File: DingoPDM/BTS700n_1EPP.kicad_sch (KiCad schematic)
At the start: 13 parts, among them U5 BTS700n-1EPP

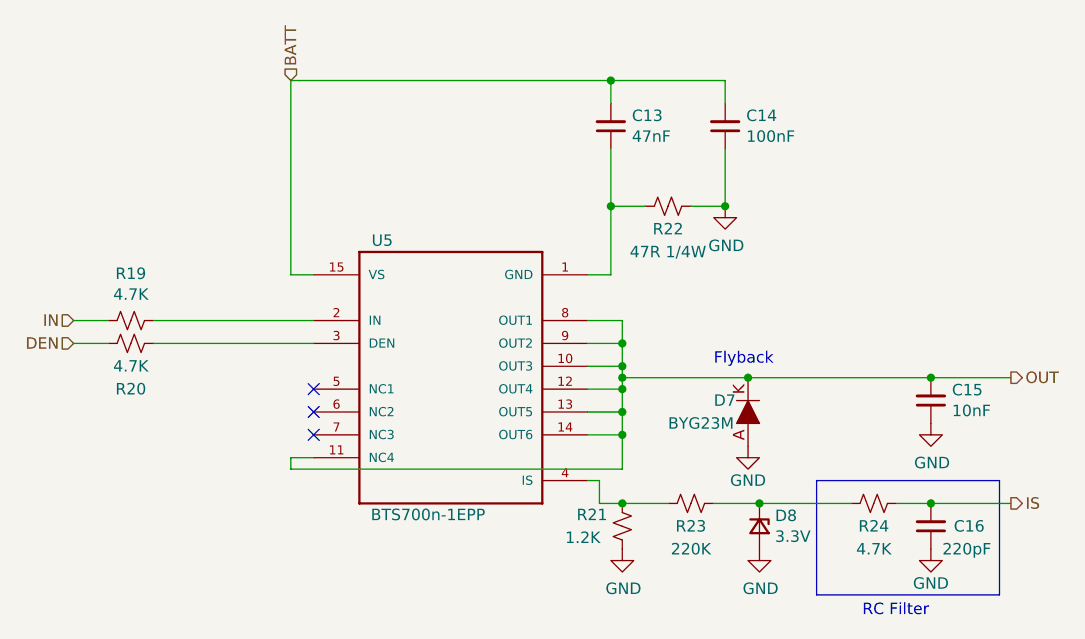
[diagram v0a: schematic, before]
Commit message: Swapped to AMPSEAL 14 pins
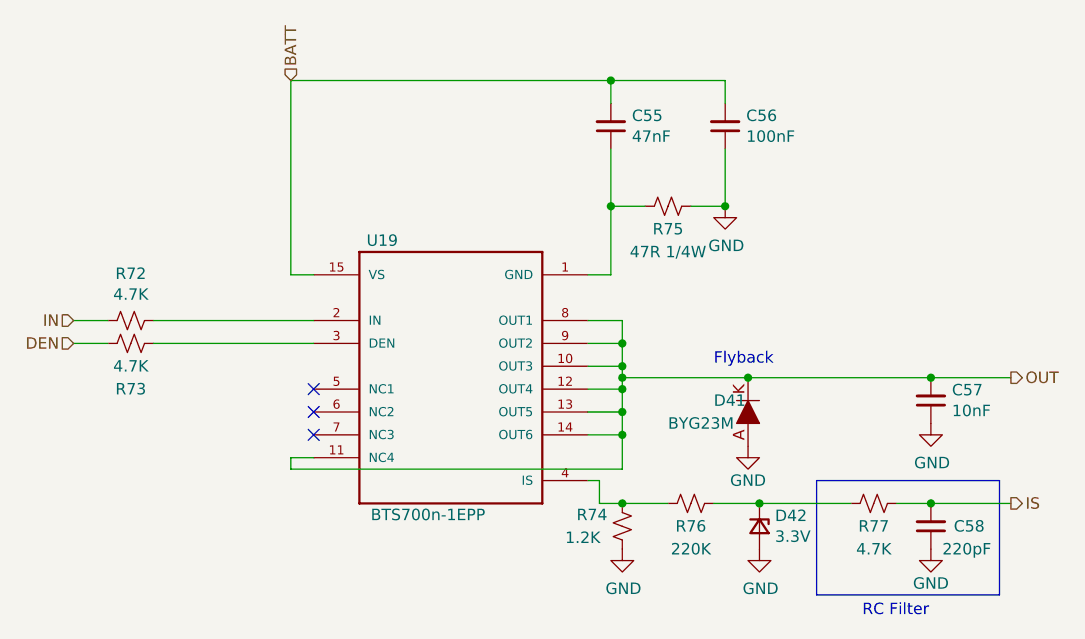
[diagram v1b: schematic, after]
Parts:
- renumbered C13 to C55, C14 to C56, C15 to C57, C16 to C58, D7 to D41, D8 to D42, R19 to R72, R20 to R73, R21 to R74, R22 to R75, R23 to R76, R24 to R77, U5 to U19
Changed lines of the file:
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@@
     (effects (font (size 1.27 1.27)) (justify right))
   )
-  (symbol (lib_id "Device:R_Small_US") (at 96.52 90.17 270)
-    (in_bom yes) (on_board yes)
-    (property "Reference" "R19" (id 0) (at 96.52 84.963 90))
+  (symbol (lib_id "Device:R_Small_US") (at 96.52 90.17 270) (unit 1)
+    (in_bom yes) (on_board yes)
+    (property "Reference" "R72" (id 0) (at 96.52 84.963 90))
     (property "Value" "4.7K" (id 1) (at 96.52 87.2744 90))
     (property "Footprint" "Resistor_SMD:R_0805_2012Metric" (id 2) (at 96.52 90.17 0)
@@
     (pin "2")
   )
-  (symbol (lib_id "Device:R_Small_US") (at 96.52 92.71 270)
-    (in_bom yes) (on_board yes)
-    (property "Reference" "R20" (id 0) (at 96.52 97.79 90))
+  (symbol (lib_id "Device:R_Small_US") (at 96.52 92.71 270) (unit 1)
+    (in_bom yes) (on_board yes)
+    (property "Reference" "R73" (id 0) (at 96.52 97.79 90))
     (property "Value" "4.7K" (id 1) (at 96.52 95.25 90))
     (property "Footprint" "Resistor_SMD:R_0805_2012Metric" (id 2) (at 96.52 92.71 0)
@@
     (pin "2")
   )
-  (symbol (lib_id "Device:C_Small") (at 162.56 68.58 180)
-    (in_bom yes) (on_board yes)
-    (property "Reference" "C14" (id 0) (at 164.8968 67.4116 0)
+  (symbol (lib_id "Device:C_Small") (at 162.56 68.58 180) (unit 1)
+    (in_bom yes) (on_board yes)
+    (property "Reference" "C56" (id 0) (at 164.8968 67.4116 0)
       (effects (font (size 1.27 1.27)) (justify right))
     )
@@
     (pin "2")
   )
-  (symbol (lib_id "Device:C_Small") (at 149.86 68.58 180)
-    (in_bom yes) (on_board yes)
-    (property "Reference" "C13" (id 0) (at 152.1968 67.4116 0)
+  (symbol (lib_id "Device:C_Small") (at 149.86 68.58 180) (unit 1)
+    (in_bom yes) (on_board yes)
+    (property "Reference" "C55" (id 0) (at 152.1968 67.4116 0)
       (effects (font (size 1.27 1.27)) (justify right))
     )
@@
     (pin "2")
   )
-  (symbol (lib_id "Device:R_Small_US") (at 156.21 77.47 270)
-    (in_bom yes) (on_board yes)
-    (property "Reference" "R22" (id 0) (at 156.21 80.01 90))
+  (symbol (lib_id "Device:R_Small_US") (at 156.21 77.47 270) (unit 1)
+    (in_bom yes) (on_board yes)
+    (property "Reference" "R75" (id 0) (at 156.21 80.01 90))
     (property "Value" "47R 1/4W" (id 1) (at 156.21 82.55 90))
     (property "Footprint" "Resistor_SMD:R_1206_3216Metric" (id 2) (at 156.21 77.47 0)
@@
     (pin "2")
   )
-  (symbol (lib_id "power:GND") (at 162.56 77.47 0)
-    (in_bom yes) (on_board yes)
-    (property "Reference" "#PWR026" (id 0) (at 162.56 83.82 0)
+  (symbol (lib_id "power:GND") (at 162.56 77.47 0) (unit 1)
+    (in_bom yes) (on_board yes)
+    (property "Reference" "#PWR0156" (id 0) (at 162.56 83.82 0)
       (effects (font (size 1.27 1.27)) hide)
     )
@@
     (pin "1")
   )
-  (symbol (lib_id "Device:C_Small") (at 185.42 99.06 180)
-    (in_bom yes) (on_board yes)
-    (property "Reference" "C15" (id 0) (at 187.7568 97.8916 0)
+  (symbol (lib_id "Device:C_Small") (at 185.42 99.06 180) (unit 1)
+    (in_bom yes) (on_board yes)
+    (property "Reference" "C57" (id 0) (at 187.7568 97.8916 0)
       (effects (font (size 1.27 1.27)) (justify right))
     )
@@
     (pin "2")
   )
-  (symbol (lib_id "power:GND") (at 185.42 101.6 0)
-    (in_bom yes) (on_board yes)
-    (property "Reference" "#PWR029" (id 0) (at 185.42 107.95 0)
+  (symbol (lib_id "power:GND") (at 185.42 101.6 0) (unit 1)
+    (in_bom yes) (on_board yes)
+    (property "Reference" "#PWR0159" (id 0) (at 185.42 107.95 0)
       (effects (font (size 1.27 1.27)) hide)
     )
@@
     (pin "1")
   )
-  (symbol (lib_id "Device:R_Small_US") (at 179.07 110.49 270)
-    (in_bom yes) (on_board yes)
-    (property "Reference" "R24" (id 0) (at 179.07 113.03 90))
+  (symbol (lib_id "Device:R_Small_US") (at 179.07 110.49 270) (unit 1)
+    (in_bom yes) (on_board yes)
+    (property "Reference" "R77" (id 0) (at 179.07 113.03 90))
     (property "Value" "4.7K" (id 1) (at 179.07 115.57 90))
     (property "Footprint" "Resistor_SMD:R_0805_2012Metric" (id 2) (at 179.07 110.49 0)
@@
     (pin "2")
   )
-  (symbol (lib_id "Device:C_Small") (at 185.42 113.03 180)
-    (in_bom yes) (on_board yes)
-    (property "Reference" "C16" (id 0) (at 187.96 113.03 0)
+  (symbol (lib_id "Device:C_Small") (at 185.42 113.03 180) (unit 1)
+    (in_bom yes) (on_board yes)
+    (property "Reference" "C58" (id 0) (at 187.96 113.03 0)
       (effects (font (size 1.27 1.27)) (justify right))
     )
@@
     (pin "2")
   )
-  (symbol (lib_id "Device:R_Small_US") (at 151.13 113.03 0)
-    (in_bom yes) (on_board yes)
-    (property "Reference" "R21" (id 0) (at 146.05 111.76 0)
+  (symbol (lib_id "Device:R_Small_US") (at 151.13 113.03 0) (unit 1)
+    (in_bom yes) (on_board yes)
+    (property "Reference" "R74" (id 0) (at 146.05 111.76 0)
       (effects (font (size 1.27 1.27)) (justify left))
     )
@@
     (pin "2")
   )
-  (symbol (lib_id "Device:R_Small_US") (at 158.75 110.49 270)
-    (in_bom yes) (on_board yes)
-    (property "Reference" "R23" (id 0) (at 158.75 113.03 90))
+  (symbol (lib_id "Device:R_Small_US") (at 158.75 110.49 270) (unit 1)
+    (in_bom yes) (on_board yes)
+    (property "Reference" "R76" (id 0) (at 158.75 113.03 90))
     (property "Value" "220K" (id 1) (at 158.75 115.57 90))
     (property "Footprint" "Resistor_SMD:R_0805_2012Metric" (id 2) (at 158.75 110.49 0)
@@
     (pin "2")
   )
-  (symbol (lib_id "Device:D_Zener_Small") (at 166.37 113.03 270)
-    (in_bom yes) (on_board yes)
-    (property "Reference" "D8" (id 0) (at 168.0972 111.8616 90)
+  (symbol (lib_id "Device:D_Zener_Small") (at 166.37 113.03 270) (unit 1)
+    (in_bom yes) (on_board yes)
+    (property "Reference" "D42" (id 0) (at 168.0972 111.8616 90)
       (effects (font (size 1.27 1.27)) (justify left))
     )
@@
     (pin "2")
   )
-  (symbol (lib_id "power:GND") (at 151.13 115.57 0)
-    (in_bom yes) (on_board yes)
-    (property "Reference" "#PWR025" (id 0) (at 151.13 121.92 0)
+  (symbol (lib_id "power:GND") (at 151.13 115.57 0) (unit 1)
+    (in_bom yes) (on_board yes)
+    (property "Reference" "#PWR0155" (id 0) (at 151.13 121.92 0)
       (effects (font (size 1.27 1.27)) hide)
     )
@@
     (pin "1")
   )
-  (symbol (lib_id "power:GND") (at 166.37 115.57 0)
-    (in_bom yes) (on_board yes)
-    (property "Reference" "#PWR028" (id 0) (at 166.37 121.92 0)
+  (symbol (lib_id "power:GND") (at 166.37 115.57 0) (unit 1)
+    (in_bom yes) (on_board yes)
+    (property "Reference" "#PWR0158" (id 0) (at 166.37 121.92 0)
       (effects (font (size 1.27 1.27)) hide)
     )
@@
     (pin "1")
   )
-  (symbol (lib_id "power:GND") (at 185.42 115.57 0)
-    (in_bom yes) (on_board yes)
-    (property "Reference" "#PWR030" (id 0) (at 185.42 121.92 0)
+  (symbol (lib_id "power:GND") (at 185.42 115.57 0) (unit 1)
+    (in_bom yes) (on_board yes)
+    (property "Reference" "#PWR0160" (id 0) (at 185.42 121.92 0)
       (effects (font (size 1.27 1.27)) hide)
     )
@@
     (pin "1")
   )
-  (symbol (lib_id "power:GND") (at 165.1 104.14 0)
-    (in_bom yes) (on_board yes)
-    (property "Reference" "#PWR027" (id 0) (at 165.1 110.49 0)
+  (symbol (lib_id "power:GND") (at 165.1 104.14 0) (unit 1)
+    (in_bom yes) (on_board yes)
+    (property "Reference" "#PWR0157" (id 0) (at 165.1 110.49 0)
       (effects (font (size 1.27 1.27)) hide)
     )
@@
     (pin "1")
   )
-  (symbol (lib_id "Profet:BTS700n-1EPP") (at 121.92 82.55 0)
-    (in_bom yes) (on_board yes)
-    (property "Reference" "U5" (id 0) (at 124.46 81.28 0))
+  (symbol (lib_id "Profet:BTS700n-1EPP") (at 121.92 82.55 0) (unit 1)
+    (in_bom yes) (on_board yes)
+    (property "Reference" "U19" (id 0) (at 124.46 81.28 0))
     (property "Value" "BTS700n-1EPP" (id 1) (at 129.54 111.76 0))
     (property "Footprint" "Profet:TDSO-14" (id 2) (at 121.92 82.55 0)
@@
     (pin "9")
   )
-  (symbol (lib_id "dk_Diodes-Rectifiers-Single:SS14") (at 165.1 99.06 270)
-    (in_bom yes) (on_board yes)
-    (property "Reference" "D7" (id 0) (at 161.29 99.06 90)
-      (effects (font (size 1.27 1.27)) (justify left))
-    )
+  (symbol (lib_id "dk_Diodes-Rectifiers-Single:SS14") (at 165.1 99.06 270) (unit 1)
+    (in_bom yes) (on_board yes)
+    (property "Reference" "D41" (id 0) (at 161.29 99.06 90)
+      (effects (font (size 1.27 1.27)) (justify left))
+    )

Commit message: Removed unused IRQs, added pd res on PF GPIO reset
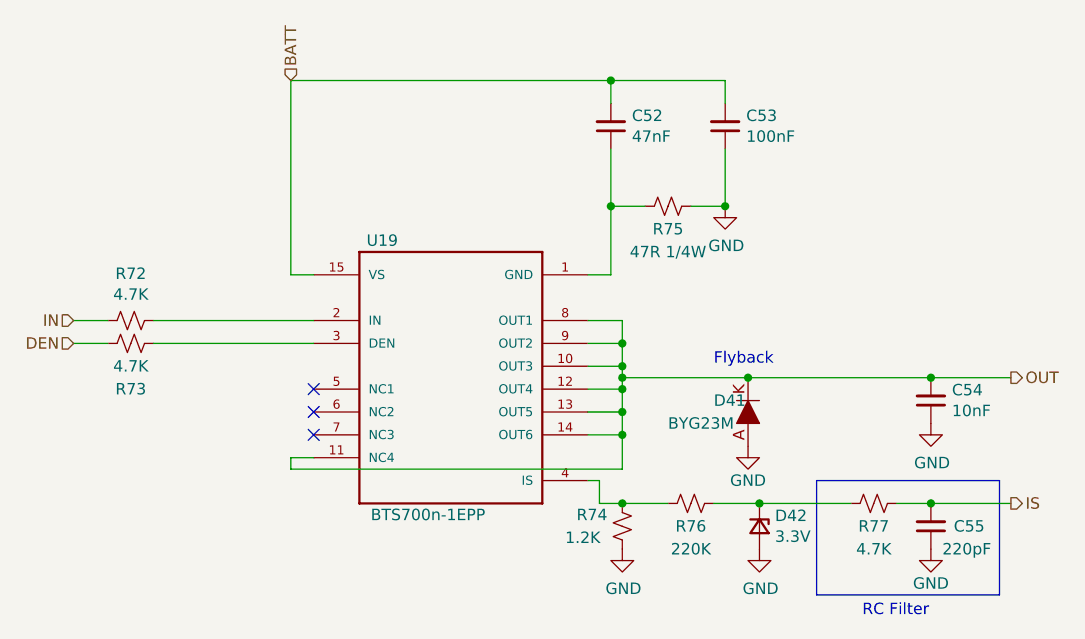
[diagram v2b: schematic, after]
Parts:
- renumbered C55 to C52, C56 to C53, C57 to C54, C58 to C55
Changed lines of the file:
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@@
   (symbol (lib_id "Device:C_Small") (at 162.56 68.58 180) (unit 1)
     (in_bom yes) (on_board yes)
-    (property "Reference" "C56" (id 0) (at 164.8968 67.4116 0)
+    (property "Reference" "C53" (id 0) (at 164.8968 67.4116 0)
       (effects (font (size 1.27 1.27)) (justify right))
     )
@@
   (symbol (lib_id "Device:C_Small") (at 149.86 68.58 180) (unit 1)
     (in_bom yes) (on_board yes)
-    (property "Reference" "C55" (id 0) (at 152.1968 67.4116 0)
+    (property "Reference" "C52" (id 0) (at 152.1968 67.4116 0)
       (effects (font (size 1.27 1.27)) (justify right))
     )
@@
   (symbol (lib_id "power:GND") (at 162.56 77.47 0) (unit 1)
     (in_bom yes) (on_board yes)
-    (property "Reference" "#PWR0156" (id 0) (at 162.56 83.82 0)
+    (property "Reference" "#PWR0153" (id 0) (at 162.56 83.82 0)
       (effects (font (size 1.27 1.27)) hide)
     )
@@
   (symbol (lib_id "Device:C_Small") (at 185.42 99.06 180) (unit 1)
     (in_bom yes) (on_board yes)
-    (property "Reference" "C57" (id 0) (at 187.7568 97.8916 0)
+    (property "Reference" "C54" (id 0) (at 187.7568 97.8916 0)
       (effects (font (size 1.27 1.27)) (justify right))
     )
@@
   (symbol (lib_id "power:GND") (at 185.42 101.6 0) (unit 1)
     (in_bom yes) (on_board yes)
-    (property "Reference" "#PWR0159" (id 0) (at 185.42 107.95 0)
+    (property "Reference" "#PWR0156" (id 0) (at 185.42 107.95 0)
       (effects (font (size 1.27 1.27)) hide)
     )
@@
   (symbol (lib_id "Device:C_Small") (at 185.42 113.03 180) (unit 1)
     (in_bom yes) (on_board yes)
-    (property "Reference" "C58" (id 0) (at 187.96 113.03 0)
+    (property "Reference" "C55" (id 0) (at 187.96 113.03 0)
       (effects (font (size 1.27 1.27)) (justify right))
     )
@@
   (symbol (lib_id "power:GND") (at 151.13 115.57 0) (unit 1)
     (in_bom yes) (on_board yes)
-    (property "Reference" "#PWR0155" (id 0) (at 151.13 121.92 0)
+    (property "Reference" "#PWR0152" (id 0) (at 151.13 121.92 0)
       (effects (font (size 1.27 1.27)) hide)
     )
@@
   (symbol (lib_id "power:GND") (at 166.37 115.57 0) (unit 1)
     (in_bom yes) (on_board yes)
-    (property "Reference" "#PWR0158" (id 0) (at 166.37 121.92 0)
+    (property "Reference" "#PWR0155" (id 0) (at 166.37 121.92 0)
       (effects (font (size 1.27 1.27)) hide)
     )
@@
   (symbol (lib_id "power:GND") (at 185.42 115.57 0) (unit 1)
     (in_bom yes) (on_board yes)
-    (property "Reference" "#PWR0160" (id 0) (at 185.42 121.92 0)
+    (property "Reference" "#PWR0157" (id 0) (at 185.42 121.92 0)
       (effects (font (size 1.27 1.27)) hide)
     )
@@
   (symbol (lib_id "power:GND") (at 165.1 104.14 0) (unit 1)
     (in_bom yes) (on_board yes)
-    (property "Reference" "#PWR0157" (id 0) (at 165.1 110.49 0)
-      (effects (font (size 1.27 1.27)) hide)
-    )
+    (property "Reference" "#PWR0154" (id 0) (at 165.1 110.49 0)
+      (effects (font (size 1.27 1.27)) hide)
+    )

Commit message: layout finished
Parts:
- renumbered C52 to C53, C53 to C54, C54 to C55, C55 to C56, D41 to D40, D42 to D41, R72 to R71, R73 to R72, R74 to R73, R75 to R74, R76 to R75, R77 to R76, U19 to U20
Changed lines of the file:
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@@
   (symbol (lib_id "Device:R_Small_US") (at 96.52 90.17 270) (unit 1)
     (in_bom yes) (on_board yes)
-    (property "Reference" "R72" (id 0) (at 96.52 84.963 90))
+    (property "Reference" "R71" (id 0) (at 96.52 84.963 90))
     (property "Value" "4.7K" (id 1) (at 96.52 87.2744 90))
     (property "Footprint" "Resistor_SMD:R_0805_2012Metric" (id 2) (at 96.52 90.17 0)
@@
   (symbol (lib_id "Device:R_Small_US") (at 96.52 92.71 270) (unit 1)
     (in_bom yes) (on_board yes)
-    (property "Reference" "R73" (id 0) (at 96.52 97.79 90))
+    (property "Reference" "R72" (id 0) (at 96.52 97.79 90))
     (property "Value" "4.7K" (id 1) (at 96.52 95.25 90))
     (property "Footprint" "Resistor_SMD:R_0805_2012Metric" (id 2) (at 96.52 92.71 0)
@@
   (symbol (lib_id "Device:C_Small") (at 162.56 68.58 180) (unit 1)
     (in_bom yes) (on_board yes)
-    (property "Reference" "C53" (id 0) (at 164.8968 67.4116 0)
+    (property "Reference" "C54" (id 0) (at 164.8968 67.4116 0)
       (effects (font (size 1.27 1.27)) (justify right))
     )
@@
   (symbol (lib_id "Device:C_Small") (at 149.86 68.58 180) (unit 1)
     (in_bom yes) (on_board yes)
-    (property "Reference" "C52" (id 0) (at 152.1968 67.4116 0)
+    (property "Reference" "C53" (id 0) (at 152.1968 67.4116 0)
       (effects (font (size 1.27 1.27)) (justify right))
     )
@@
   (symbol (lib_id "Device:R_Small_US") (at 156.21 77.47 270) (unit 1)
     (in_bom yes) (on_board yes)
-    (property "Reference" "R75" (id 0) (at 156.21 80.01 90))
+    (property "Reference" "R74" (id 0) (at 156.21 80.01 90))
     (property "Value" "47R 1/4W" (id 1) (at 156.21 82.55 90))
     (property "Footprint" "Resistor_SMD:R_1206_3216Metric" (id 2) (at 156.21 77.47 0)
@@
   (symbol (lib_id "power:GND") (at 162.56 77.47 0) (unit 1)
     (in_bom yes) (on_board yes)
-    (property "Reference" "#PWR0153" (id 0) (at 162.56 83.82 0)
+    (property "Reference" "#PWR0154" (id 0) (at 162.56 83.82 0)
       (effects (font (size 1.27 1.27)) hide)
     )
@@
   (symbol (lib_id "Device:C_Small") (at 185.42 99.06 180) (unit 1)
     (in_bom yes) (on_board yes)
-    (property "Reference" "C54" (id 0) (at 187.7568 97.8916 0)
+    (property "Reference" "C55" (id 0) (at 187.7568 97.8916 0)
       (effects (font (size 1.27 1.27)) (justify right))
     )
@@
   (symbol (lib_id "power:GND") (at 185.42 101.6 0) (unit 1)
     (in_bom yes) (on_board yes)
-    (property "Reference" "#PWR0156" (id 0) (at 185.42 107.95 0)
+    (property "Reference" "#PWR0157" (id 0) (at 185.42 107.95 0)
       (effects (font (size 1.27 1.27)) hide)
     )
@@
   (symbol (lib_id "Device:R_Small_US") (at 179.07 110.49 270) (unit 1)
     (in_bom yes) (on_board yes)
-    (property "Reference" "R77" (id 0) (at 179.07 113.03 90))
+    (property "Reference" "R76" (id 0) (at 179.07 113.03 90))
     (property "Value" "4.7K" (id 1) (at 179.07 115.57 90))
     (property "Footprint" "Resistor_SMD:R_0805_2012Metric" (id 2) (at 179.07 110.49 0)
@@
   (symbol (lib_id "Device:C_Small") (at 185.42 113.03 180) (unit 1)
     (in_bom yes) (on_board yes)
-    (property "Reference" "C55" (id 0) (at 187.96 113.03 0)
+    (property "Reference" "C56" (id 0) (at 187.96 113.03 0)
       (effects (font (size 1.27 1.27)) (justify right))
     )
@@
   (symbol (lib_id "Device:R_Small_US") (at 151.13 113.03 0) (unit 1)
     (in_bom yes) (on_board yes)
-    (property "Reference" "R74" (id 0) (at 146.05 111.76 0)
+    (property "Reference" "R73" (id 0) (at 146.05 111.76 0)
       (effects (font (size 1.27 1.27)) (justify left))
     )
@@
   (symbol (lib_id "Device:R_Small_US") (at 158.75 110.49 270) (unit 1)
     (in_bom yes) (on_board yes)
-    (property "Reference" "R76" (id 0) (at 158.75 113.03 90))
+    (property "Reference" "R75" (id 0) (at 158.75 113.03 90))
     (property "Value" "220K" (id 1) (at 158.75 115.57 90))
     (property "Footprint" "Resistor_SMD:R_0805_2012Metric" (id 2) (at 158.75 110.49 0)
@@
   (symbol (lib_id "Device:D_Zener_Small") (at 166.37 113.03 270) (unit 1)
     (in_bom yes) (on_board yes)
-    (property "Reference" "D42" (id 0) (at 168.0972 111.8616 90)
+    (property "Reference" "D41" (id 0) (at 168.0972 111.8616 90)
       (effects (font (size 1.27 1.27)) (justify left))
     )
@@
   (symbol (lib_id "power:GND") (at 151.13 115.57 0) (unit 1)
     (in_bom yes) (on_board yes)
-    (property "Reference" "#PWR0152" (id 0) (at 151.13 121.92 0)
+    (property "Reference" "#PWR0153" (id 0) (at 151.13 121.92 0)
       (effects (font (size 1.27 1.27)) hide)
     )
@@
   (symbol (lib_id "power:GND") (at 166.37 115.57 0) (unit 1)
     (in_bom yes) (on_board yes)
-    (property "Reference" "#PWR0155" (id 0) (at 166.37 121.92 0)
+    (property "Reference" "#PWR0156" (id 0) (at 166.37 121.92 0)
       (effects (font (size 1.27 1.27)) hide)
     )
@@
   (symbol (lib_id "power:GND") (at 185.42 115.57 0) (unit 1)
     (in_bom yes) (on_board yes)
-    (property "Reference" "#PWR0157" (id 0) (at 185.42 121.92 0)
+    (property "Reference" "#PWR0158" (id 0) (at 185.42 121.92 0)
       (effects (font (size 1.27 1.27)) hide)
     )
@@
   (symbol (lib_id "power:GND") (at 165.1 104.14 0) (unit 1)
     (in_bom yes) (on_board yes)
-    (property "Reference" "#PWR0154" (id 0) (at 165.1 110.49 0)
+    (property "Reference" "#PWR0155" (id 0) (at 165.1 110.49 0)
       (effects (font (size 1.27 1.27)) hide)
     )
@@
   (symbol (lib_id "Profet:BTS700n-1EPP") (at 121.92 82.55 0) (unit 1)
     (in_bom yes) (on_board yes)
-    (property "Reference" "U19" (id 0) (at 124.46 81.28 0))
+    (property "Reference" "U20" (id 0) (at 124.46 81.28 0))
     (property "Value" "BTS700n-1EPP" (id 1) (at 129.54 111.76 0))
     (property "Footprint" "Profet:TDSO-14" (id 2) (at 121.92 82.55 0)
@@
   (symbol (lib_id "dk_Diodes-Rectifiers-Single:SS14") (at 165.1 99.06 270) (unit 1)
     (in_bom yes) (on_board yes)
-    (property "Reference" "D41" (id 0) (at 161.29 99.06 90)
-      (effects (font (size 1.27 1.27)) (justify left))
-    )
+    (property "Reference" "D40" (id 0) (at 161.29 99.06 90)
+      (effects (font (size 1.27 1.27)) (justify left))
+    )
